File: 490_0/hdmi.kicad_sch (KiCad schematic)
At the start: 8 parts, among them J25 HDMI_D_1.4, U23 ECMF04-4HSWM10, U24 ECMF04-4HSWM10

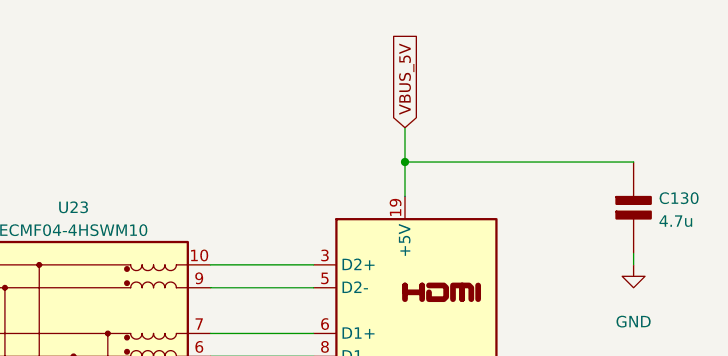
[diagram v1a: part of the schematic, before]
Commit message: Changed some local labels to the right format
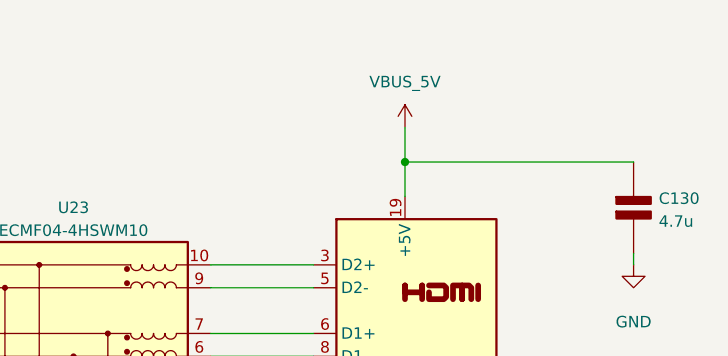
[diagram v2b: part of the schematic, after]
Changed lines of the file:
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@@
-		)
-	)
-	(global_label "VBUS_5V"
-		(shape input)
-		(at 147.32 26.67 90)
-		(fields_autoplaced yes)
-		(effects
-			(font
-				(size 1.27 1.27)
-			)
-			(justify left)
-		)
-		(property "Intersheetrefs" "${INTERSHEET_REFS}"
-			(at 147.32 15.5205 90)
-			(effects
-				(font
-					(size 1.27 1.27)
-				)
-				(justify left)
-				(hide yes)
-			)
 		)
 	)
@@
 					(unit 1)
 				)
+			)
+		)
+	)
+	(symbol
+		(lib_id "power:+3.3V")
+		(at 147.32 26.67 0)
+		(unit 1)
+		(exclude_from_sim no)
+		(in_bom yes)
+		(on_board yes)
+		(dnp no)
+		(fields_autoplaced yes)
+		(property "Reference" "#PWR020"
+			(at 147.32 30.48 0)
+			(effects
+				(font
+					(size 1.27 1.27)
+				)
+				(hide yes)
+			)
+		)
+		(property "Value" "VBUS_5V"
+			(at 147.32 21.59 0)
+			(effects
+				(font
+					(size 1.27 1.27)
+				)
+			)
+		)
+		(property "Footprint" ""
+			(at 147.32 26.67 0)
+			(effects
+				(font
+					(size 1.27 1.27)
+				)
+				(hide yes)
+			)
+		)
+		(property "Datasheet" ""
+			(at 147.32 26.67 0)
+			(effects
+				(font
+					(size 1.27 1.27)
+				)
+				(hide yes)
+			)
+		)
+		(property "Description" "Power symbol creates a global label with name \"+3.3V\""
+			(at 147.32 26.67 0)
+			(effects
+				(font
+					(size 1.27 1.27)
+				)
+				(hide yes)
+			)
+		)
+		(pin "1"
+		)
+		(instances
+			(project "490_0"
+				(path "/365a82ed-827d-43e1-aa2f-b98221c4179c/c44da2de-7309-4c48-b0b5-1c312aeb25a1"
+					(reference "#PWR020")
+					(unit 1)
+				)

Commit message: Minor updates
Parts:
- renumbered C130 to C14, C128 to C15, C129 to C16, D38 to D8, D39 to D9, J25 to J10, U23 to U5, U24 to U6

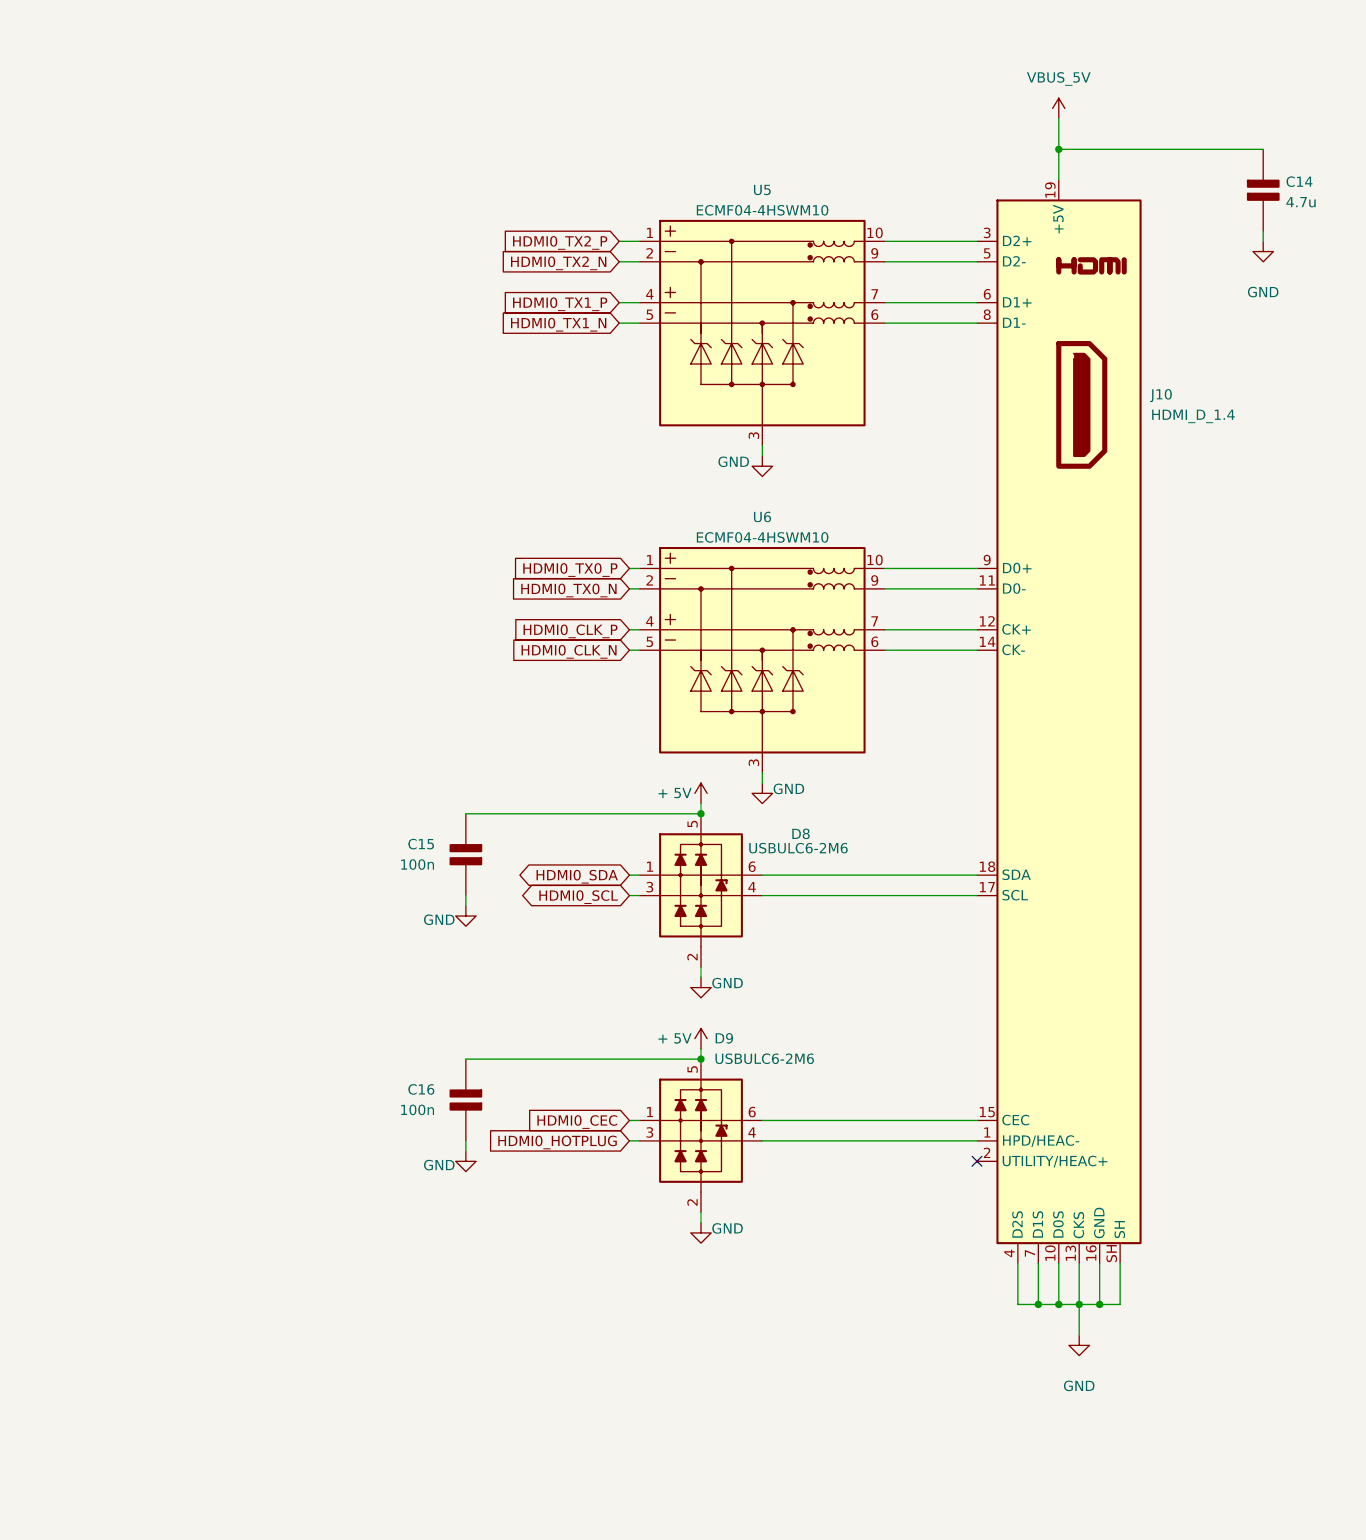
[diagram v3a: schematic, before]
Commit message: BOM + ESD replacement for HDMI
Started BOM and changed ESD chips that were obsolete. Also added 2 pin connectors
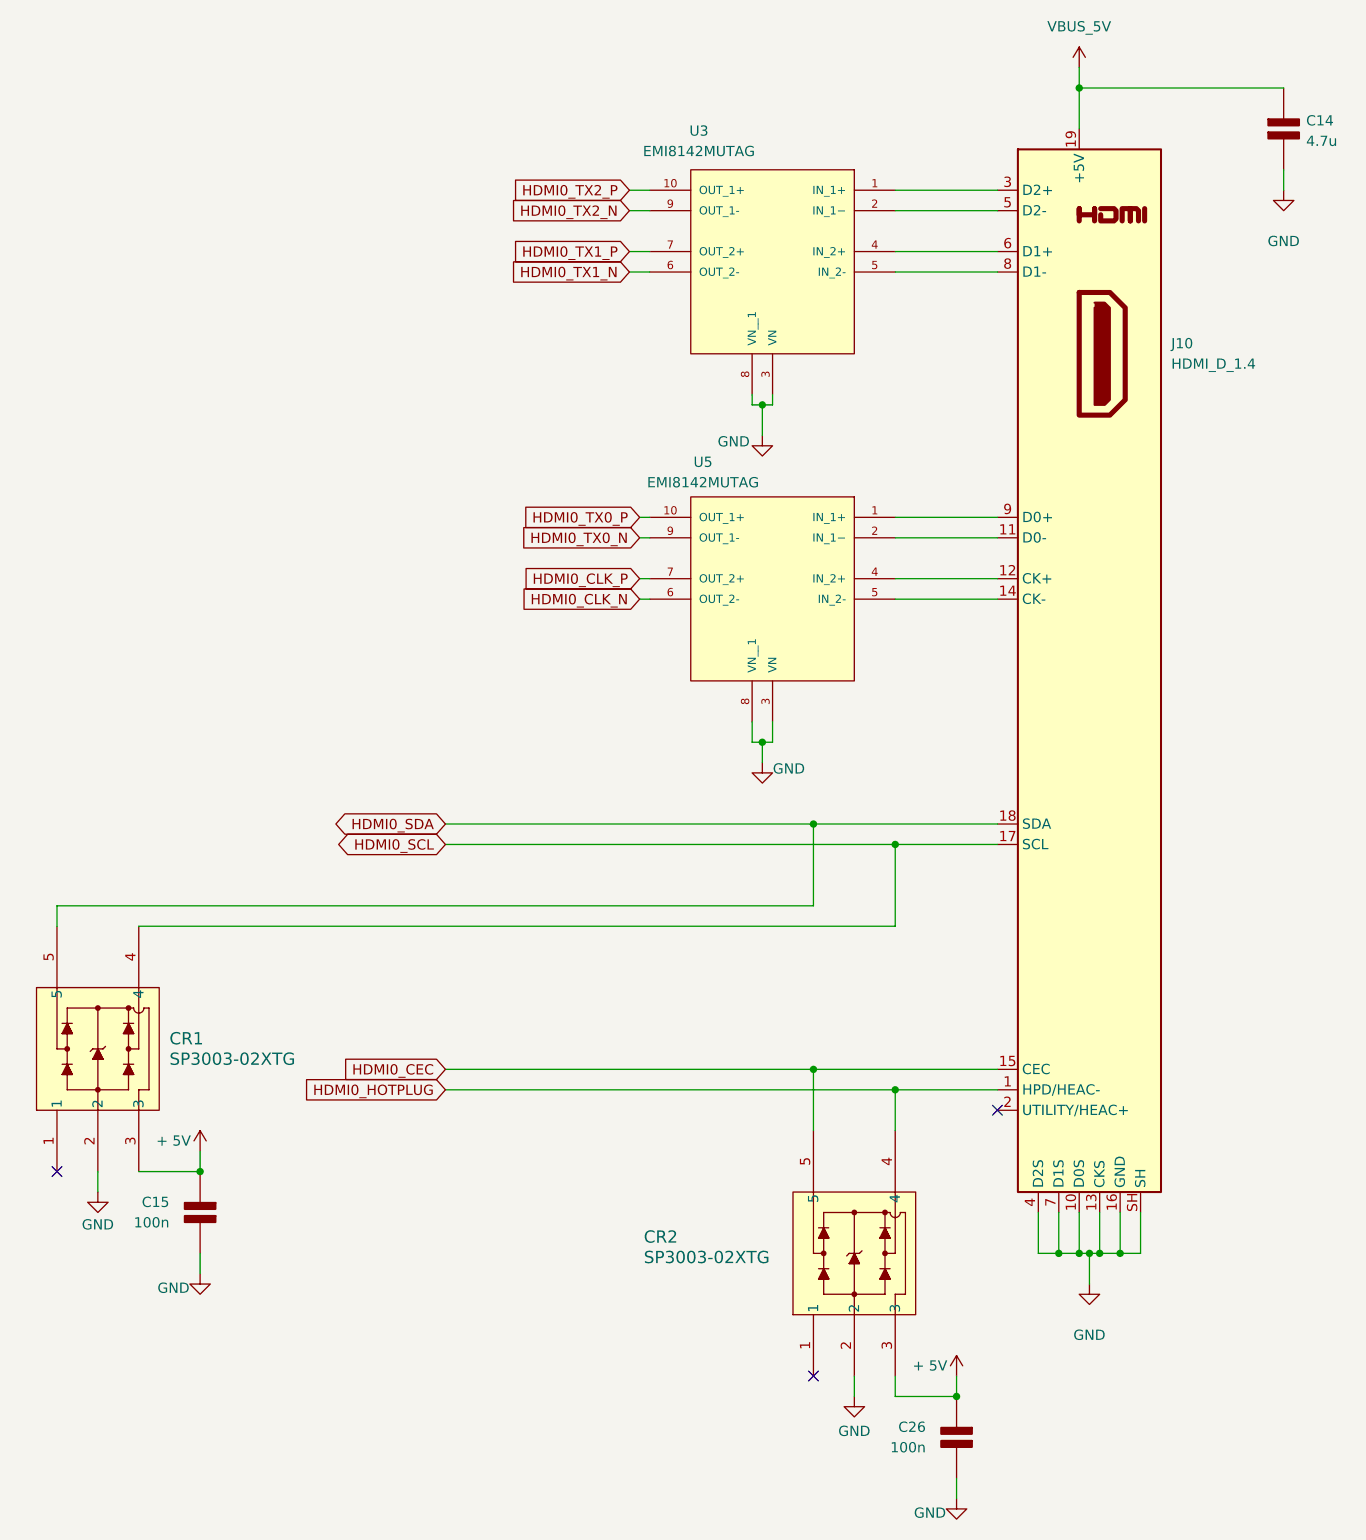
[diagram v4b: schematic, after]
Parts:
- removed C16: 100n, symbol PCM_Elektuur:C
- removed D8, D9: USBULC6-2M6, PCM_Package_TO_SOT_SMD_AKL:SOT-666, symbol PCM_Diode_TVS_AKL:USBLC6-2P6
- removed U5, U6: ECMF04-4HSWM10, Package_DFN_QFN:UDFN-10_1.35x2.6mm_P0.5mm, symbol Power_Protection:ECMF04-4HSWM10
- added C26: 100n, symbol PCM_Elektuur:C
- added CR1, CR2: SP3003-02XTG, SOT553_LTF, symbol capstone_parts:SP3003-02XTG
- added U3, U5: EMI8142MUTAG, EMI8142MUTAG:SON40P220X135X50-10N, symbol capstone_parts:EMI8142MUTAG
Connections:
- net + 5V: now also C26.1 (+), CR1.3, CR2.3
- net GND: now also C26.2 (-), CR1.2, CR2.2, U3.3 (VN), U3.8 (VN__1), U5.3 (VN), U5.8 (VN__1)
- net HDMI0_CEC: now also J10.15 (CEC), CR2.5
- net HDMI0_CLK_N: now also U5.6 (OUT_2-)
- net HDMI0_CLK_P: now also U5.7 (OUT_2+)
- net HDMI0_HOTPLUG: now also J10.1 (HPD/HEAC-), CR2.4
- net HDMI0_SCL: now also J10.17 (SCL), CR1.4
- net HDMI0_SDA: now also J10.18 (SDA), CR1.5
- net HDMI0_TX0_N: now also U5.9 (OUT_1-)
- net HDMI0_TX0_P: now also U5.10 (OUT_1+)
- net HDMI0_TX1_N: now also U3.6 (OUT_2-)
- net HDMI0_TX1_P: now also U3.7 (OUT_2+)
- net HDMI0_TX2_N: now also U3.9 (OUT_1-)
- net HDMI0_TX2_P: now also U3.10 (OUT_1+)
- net at J10.3 (D2+): now also U3.1 (IN_1+)
- net at J10.8 (D1-): now also U3.5 (IN_2-)
- net at J10.6 (D1+): now also U3.4 (IN_2+)
- net at J10.5 (D2-): now also U3.2 (IN_1−)
- net at J10.9 (D0+): now also U5.1 (IN_1+)
- net at J10.14 (CK-): now also U5.5 (IN_2-)
- net at J10.12 (CK+): now also U5.4 (IN_2+)
- net at J10.11 (D0-): now also U5.2 (IN_1−)
- no-connect marks 1 -> 3
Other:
- moved on the sheet: C14, J10

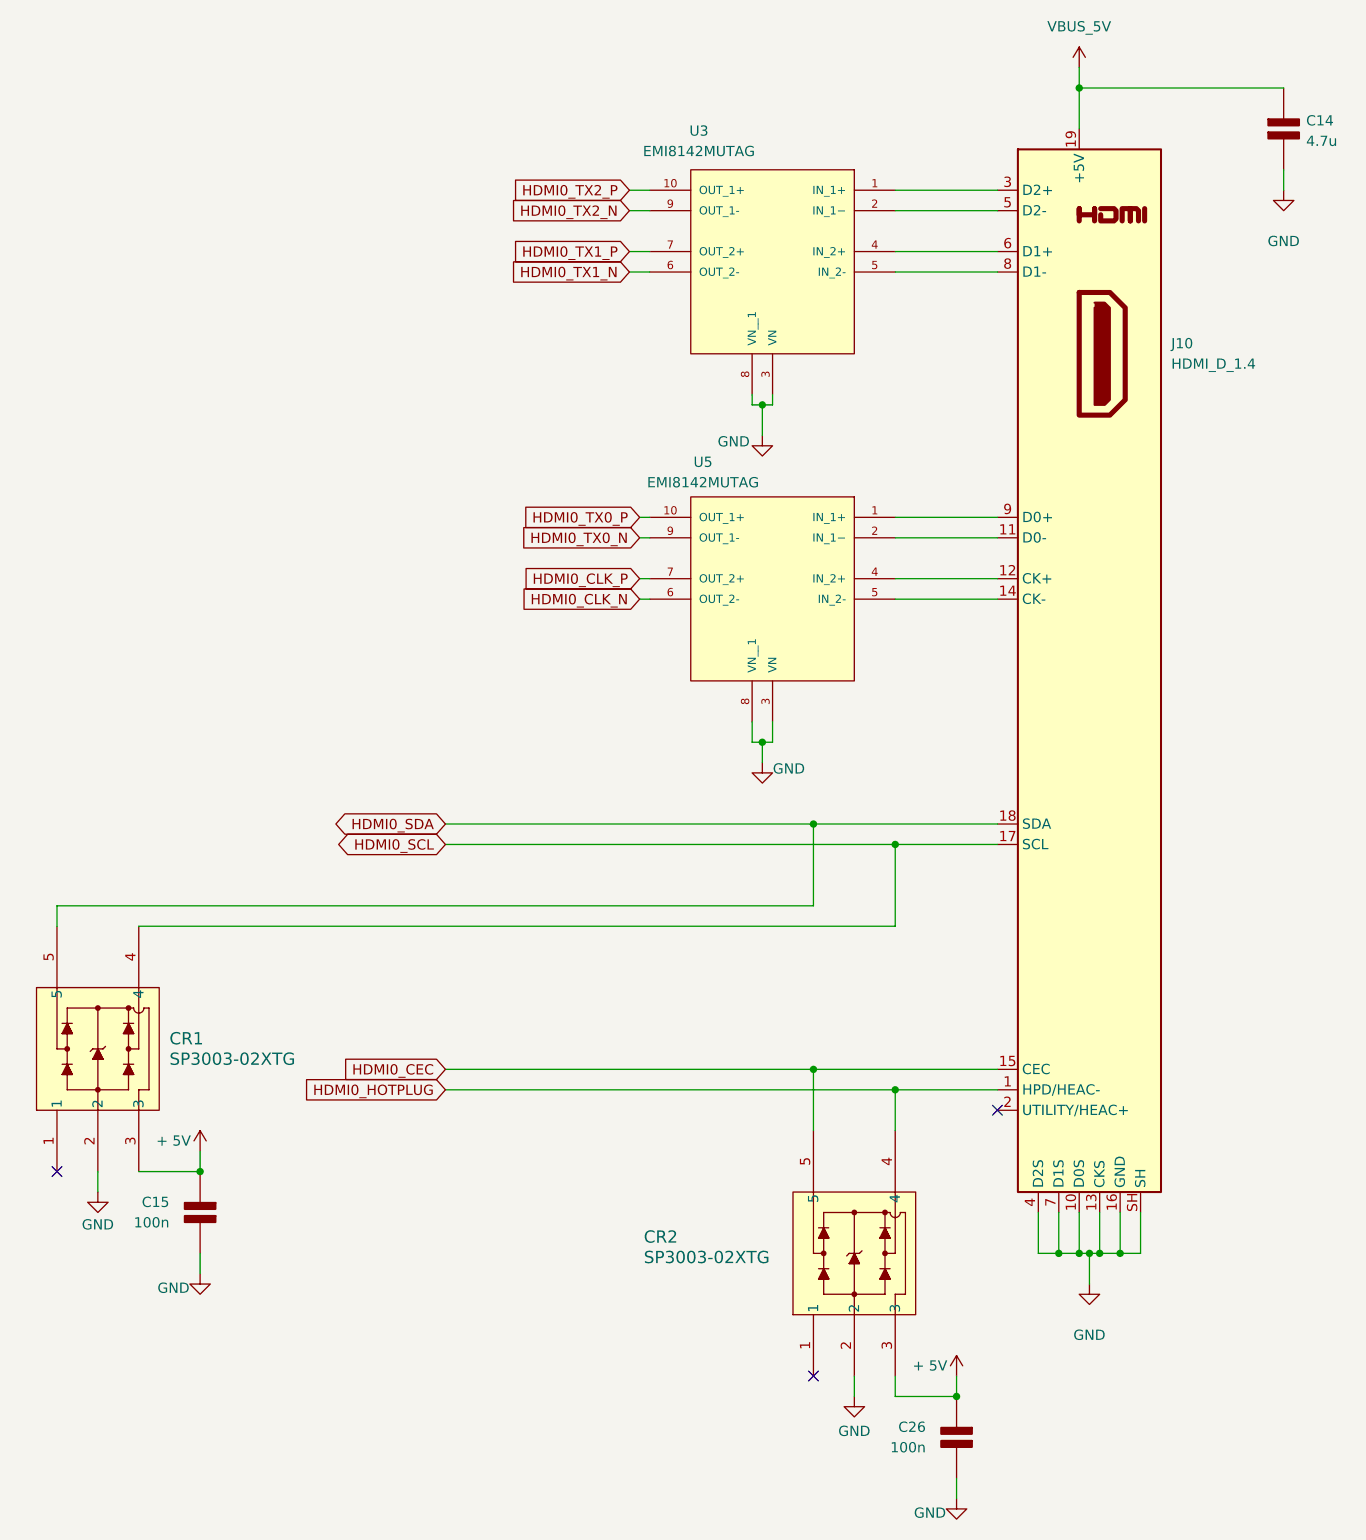
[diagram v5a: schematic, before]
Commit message: Schematic layout update
- applied hierarchical labels
- cleaned up the schematic
- finalized CM4 connections
- checked cm4 connections
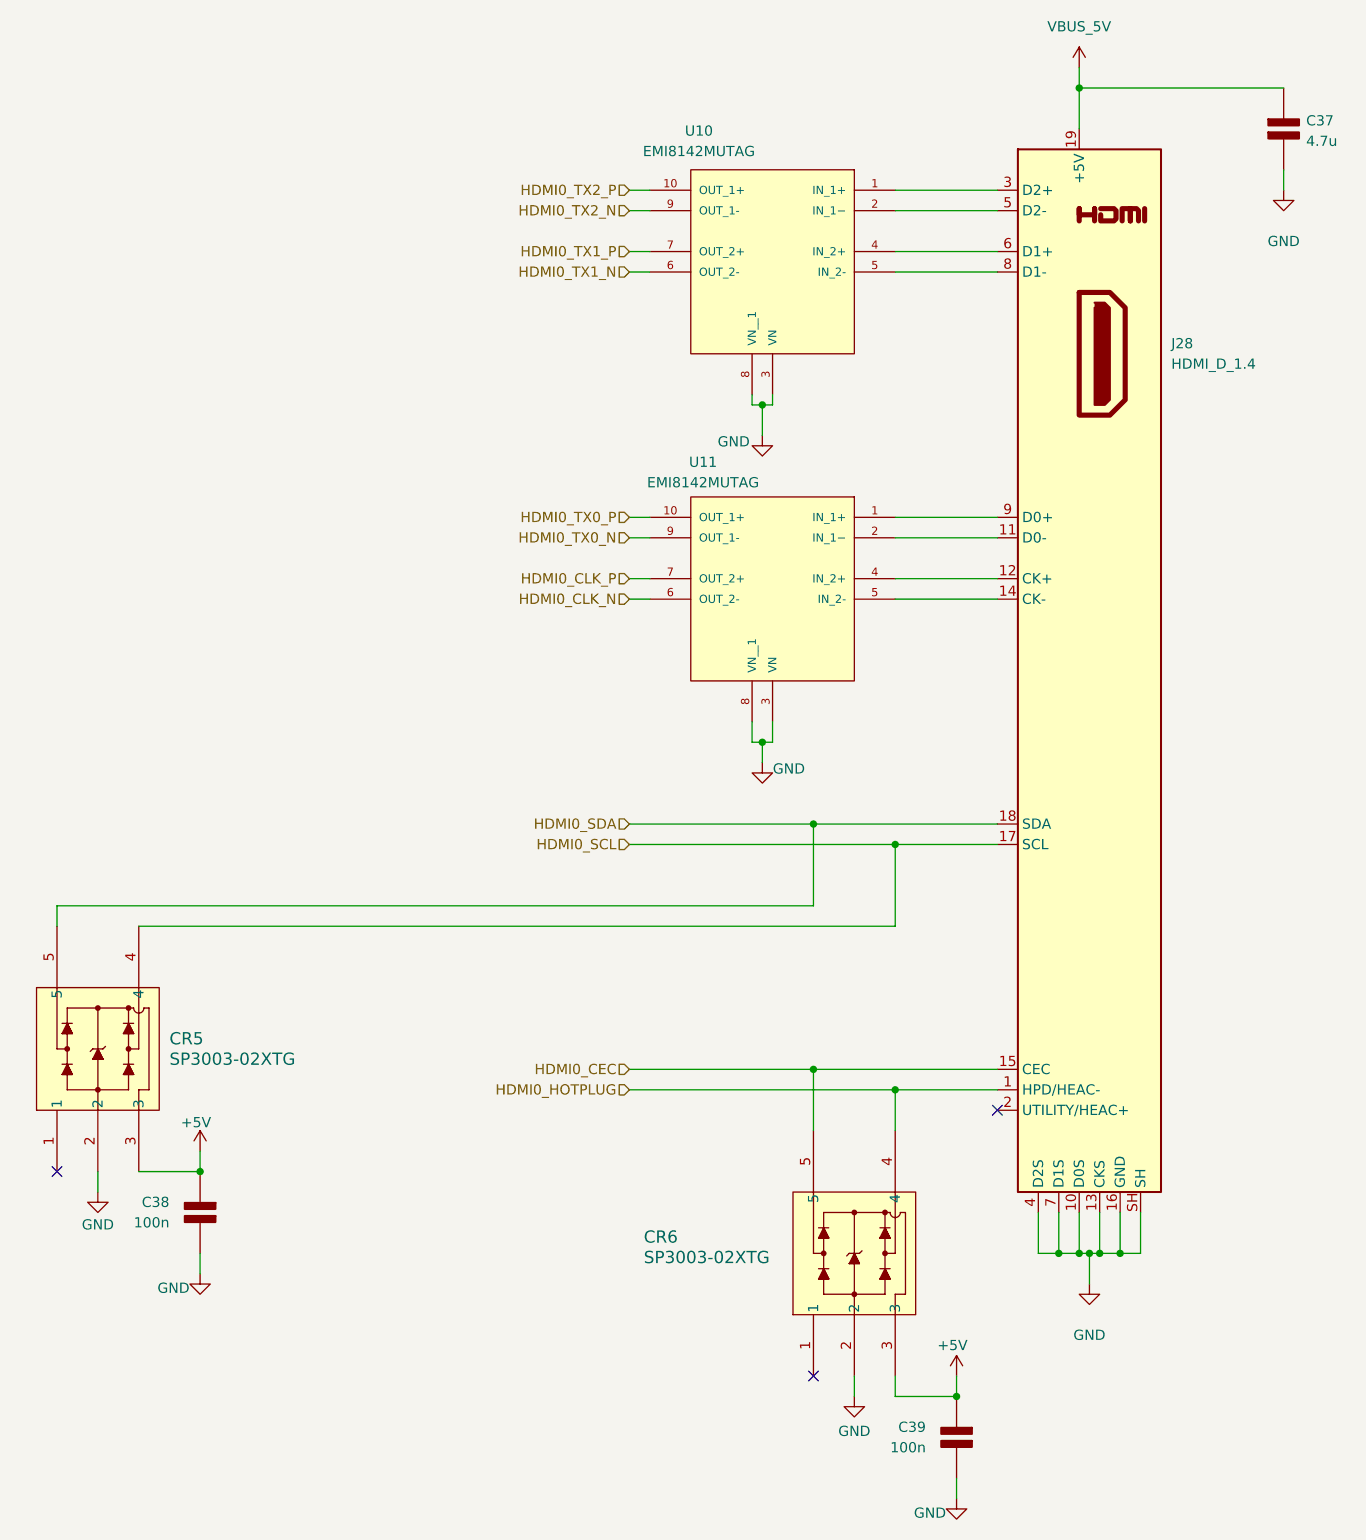
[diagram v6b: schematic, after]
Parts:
- renumbered C14 to C37, C15 to C38, C26 to C39, CR1 to CR5, CR2 to CR6, J10 to J28, U3 to U10, U5 to U11
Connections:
- net + 5V renamed +5V
